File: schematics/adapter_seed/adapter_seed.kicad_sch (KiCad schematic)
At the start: 2 parts, among them J1 Conn_02x20_Odd_Even

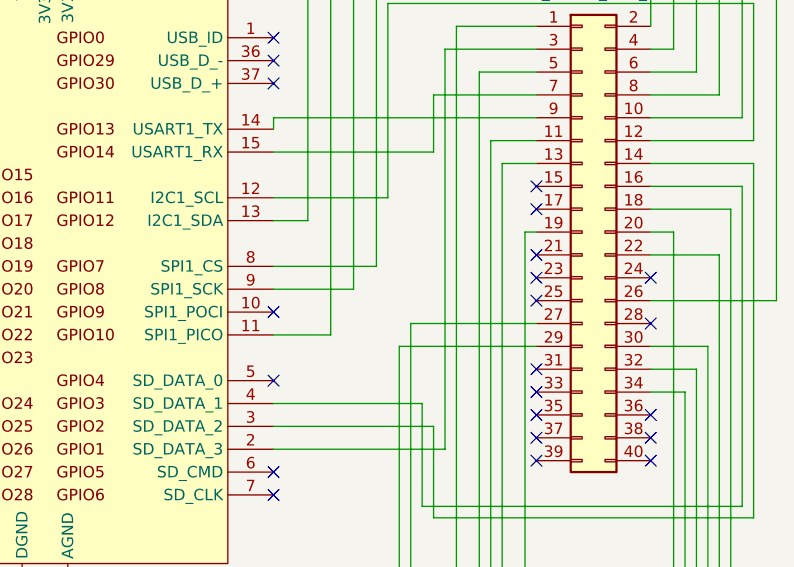
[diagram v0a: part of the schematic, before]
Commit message: avr flasher: schematic changes
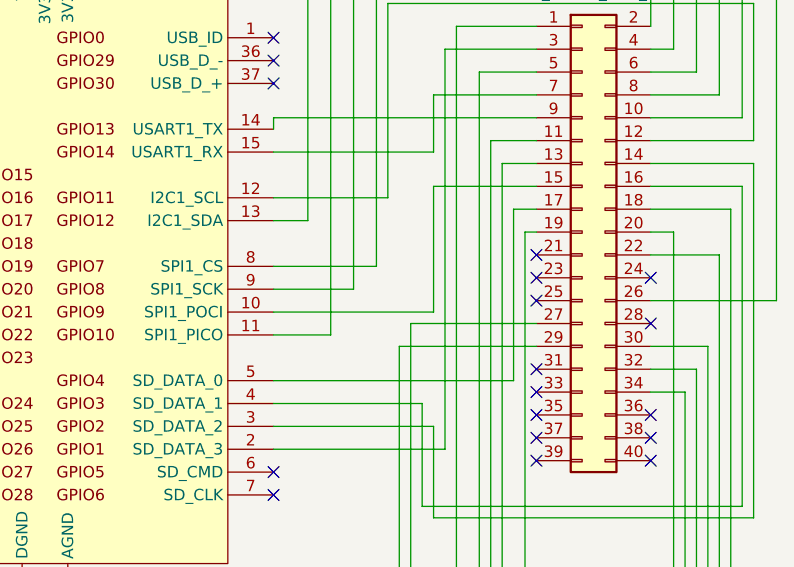
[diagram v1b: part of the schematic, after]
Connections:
- net at J1.15 (Pin_15): now also A1.10 (SPI1_POCI)
- net at J1.17 (Pin_17): now also A1.5 (SD_DATA_0)
- no-connect marks 29 -> 25
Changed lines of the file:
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@@
-	)
-	(no_connect
-		(at 146.05 95.25)
 	)
 	(no_connect
@@
 	)
 	(no_connect
-		(at 146.05 97.79)
-	)
-	(no_connect
 		(at 66.04 114.3)
-	)
-	(no_connect
-		(at 116.84 116.84)
 	)
 	(no_connect
@@
 		(at 158.75 110.49)
 	)
-	(no_connect
-		(at 116.84 109.22)
-	)
 	(wire
 		(pts
@@
 	(wire
 		(pts
+			(xy 143.51 116.84) (xy 143.51 97.79)
+		)
+		(stroke
+			(width 0)
+			(type default)
+		)
+	)
+	(wire
+		(pts
 			(xy 163.83 82.55) (xy 163.83 67.31)
 		)
@@
 	(wire
 		(pts
+			(xy 116.84 109.22) (xy 134.62 109.22)
+		)
+		(stroke
+			(width 0)
+			(type default)
+		)
+	)
+	(wire
+		(pts
 			(xy 158.75 118.11) (xy 162.56 118.11)
 		)
@@
 	(wire
 		(pts
+			(xy 134.62 109.22) (xy 134.62 95.25)
+		)
+		(stroke
+			(width 0)
+			(type default)
+		)
+	)
+	(wire
+		(pts
 			(xy 134.62 121.92) (xy 116.84 121.92)
 		)
@@
 	(wire
 		(pts
+			(xy 134.62 95.25) (xy 146.05 95.25)
+		)
+		(stroke
+			(width 0)
+			(type default)
+		)
+	)
+	(wire
+		(pts
 			(xy 158.75 107.95) (xy 172.72 107.95)
 		)
@@
 	(wire
 		(pts
+			(xy 116.84 116.84) (xy 143.51 116.84)
+		)
+		(stroke
+			(width 0)
+			(type default)
+		)
+	)
+	(wire
+		(pts
 			(xy 144.78 100.33) (xy 144.78 142.24)
 		)
@@
 		)
 		(stroke
+			(width 0)
+			(type default)
+		)
+	)
+	(wire
+		(pts
+			(xy 143.51 97.79) (xy 146.05 97.79)
+		)
+		(stroke
